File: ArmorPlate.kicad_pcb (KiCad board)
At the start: 2 copper layers, 134 x 124.5 mm, 47 parts, among them SW1 SW_Nidec_CAS-120A1, SW2 SW_Nidec_CAS-120A1

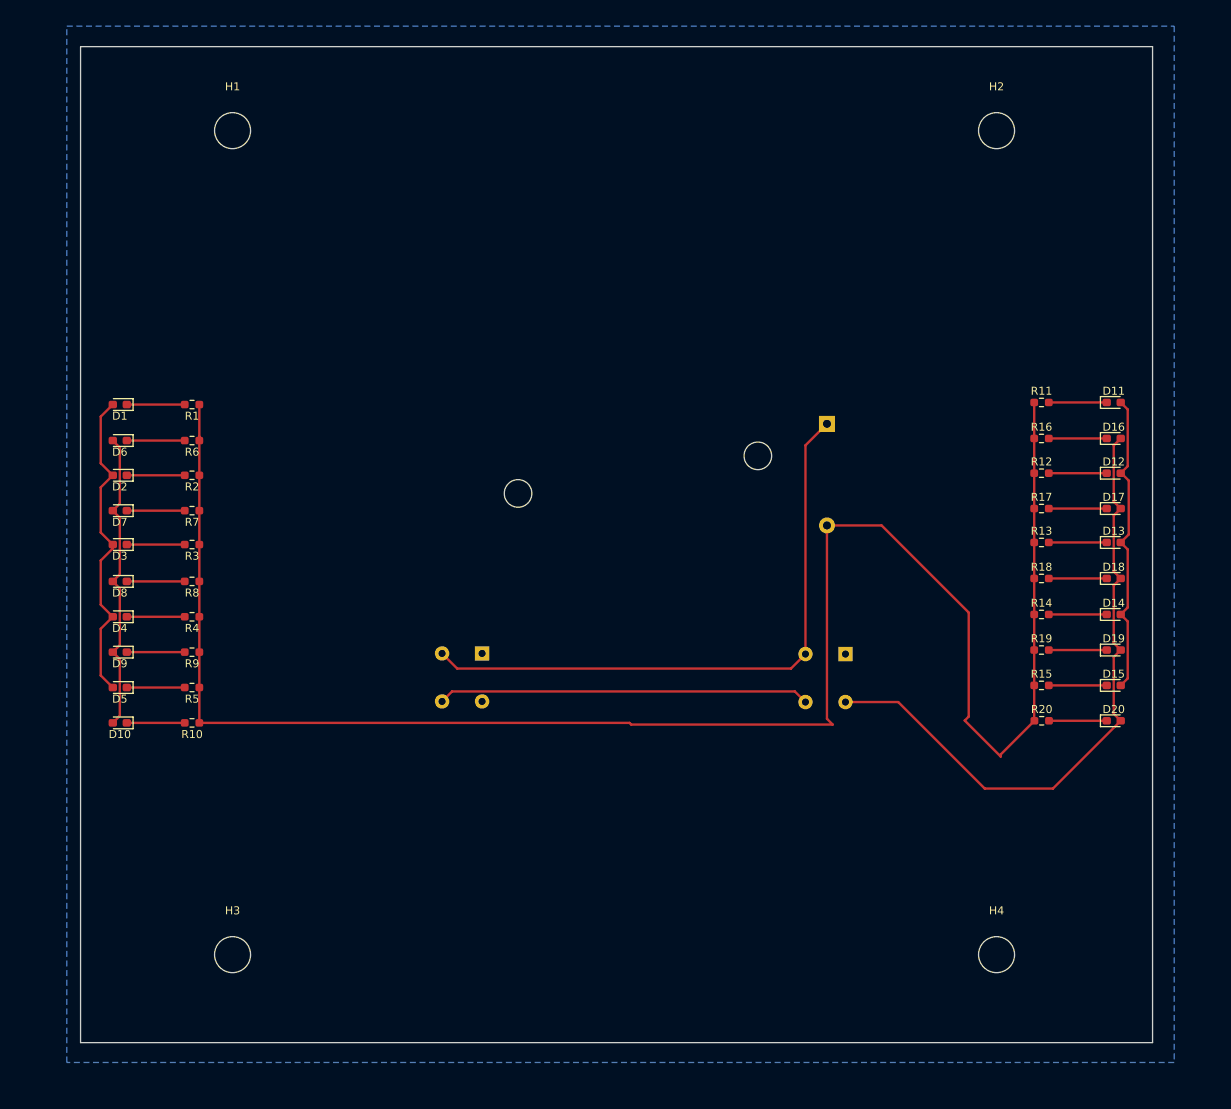
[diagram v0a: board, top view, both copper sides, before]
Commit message: updated pcb footprint for armorplate
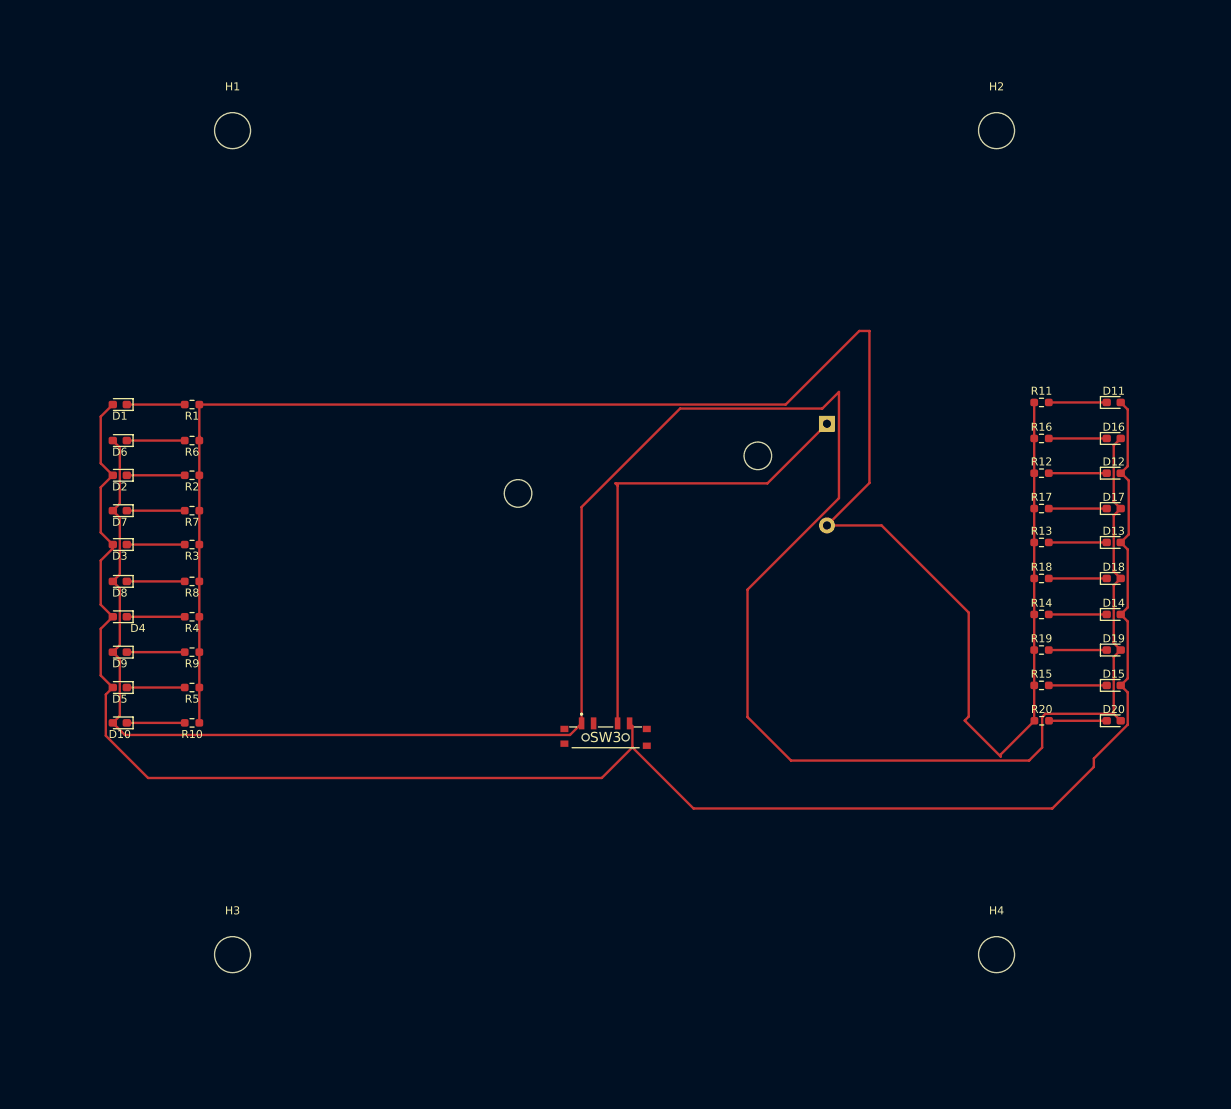
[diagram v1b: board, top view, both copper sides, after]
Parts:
- removed SW1, SW2: SW_Nidec_CAS-120A1, Button_Switch_THT:SW_Push_2P1T_Toggle_CK_PVA1xxH1xxxxxxV2
- added SW3: SW_SP3T, robomaster_footprints:EG1315AA, F.Cu at (148.6, 116.8)
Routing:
- net /3V blue: track 118.8 -> 299.4 mm
- net /3V Red: track 78.8 -> 233.2 mm
- net (no net): track 46.5 -> 0.00 mm
- net Net-(BT1-+): track 76.8 -> 59.6 mm
- net GND: track 233.1 -> 242.7 mm
- removed copper zone on B.Cu, net GND
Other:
- board outline removed

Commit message: final armorplate pcb with sp3t toggle switch
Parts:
- moved H2 0.89 mm to (196.9, 40.3)
- moved H1 0.89 mm to (102.5, 40.3)
- moved H4 0.89 mm to (196.9, 144.7)
- moved H3 0.89 mm to (102.5, 144.7)
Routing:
- added copper zone on B.Cu, net GND
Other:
- board outline added: 135 x 125.1 mm
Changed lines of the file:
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@@
 	(footprint "MountingHole:MountingHole_4.5mm"
 		(layer "F.Cu")
-		(at 102 144)
+		(at 102.55 144.7)
 		(descr "Mounting Hole 4.5mm, no annular")
 		(tags "mounting hole 4.5mm no annular")
@@
 	(footprint "MountingHole:MountingHole_4.5mm"
 		(layer "F.Cu")
-		(at 102 41)
+		(at 102.55 40.3)
 		(descr "Mounting Hole 4.5mm, no annular")
 		(tags "mounting hole 4.5mm no annular")
@@
 	(footprint "MountingHole:MountingHole_4.5mm"
 		(layer "F.Cu")
-		(at 197.5 41)
+		(at 196.95 40.3)
 		(descr "Mounting Hole 4.5mm, no annular")
 		(tags "mounting hole 4.5mm no annular")
@@
 	(footprint "MountingHole:MountingHole_4.5mm"
 		(layer "F.Cu")
-		(at 197.5 144)
+		(at 196.95 144.7)
 		(descr "Mounting Hole 4.5mm, no annular")
 		(tags "mounting hole 4.5mm no annular")
@@
 		)
 	)
+	(gr_arc
+		(start 217.55 150.745)
+		(mid 216.231981 153.926981)
+		(end 213.05 155.245)
+		(stroke
+			(width 0.05)
+			(type default)
+		)
+		(layer "Edge.Cuts")
+	)
+	(gr_arc
+		(start 213.05 30.175)
+		(mid 216.231981 31.493019)
+		(end 217.55 34.675)
+		(stroke
+			(width 0.05)
+			(type default)
+		)
+		(layer "Edge.Cuts")
+	)
+	(gr_line
+		(start 217.55 34.675)
+		(end 217.55 150.745)
+		(stroke
+			(width 0.05)
+			(type default)
+		)
+		(layer "Edge.Cuts")
+	)
+	(gr_line
+		(start 82.55 150.745)
+		(end 82.55 34.675)
+		(stroke
+			(width 0.05)
+			(type default)
+		)
+		(layer "Edge.Cuts")
+	)
+	(gr_arc
+		(start 82.55 34.675)
+		(mid 83.868019 31.493019)
+		(end 87.05 30.175)
+		(stroke
+			(width 0.05)
+			(type default)
+		)
+		(layer "Edge.Cuts")
+	)
+	(gr_line
+		(start 213.05 155.245)
+		(end 87.05 155.245)
+		(stroke
+			(width 0.05)
+			(type default)
+		)
+		(layer "Edge.Cuts")
+	)
+	(gr_line
+		(start 87.05 30.175)
+		(end 213.05 30.175)
+		(stroke
+			(width 0.05)
+			(type default)
+		)
+		(layer "Edge.Cuts")
+	)
+	(gr_arc
+		(start 87.05 155.245)
+		(mid 83.868019 153.926981)
+		(end 82.55 150.745)
+		(stroke
+			(width 0.05)
+			(type default)
+		)
+		(layer "Edge.Cuts")
+	)
 	(segment
 		(start 97.845 88.503337)
@@
 		(net 24)
 	)
+	(zone
+		(net 1)
+		(net_name "GND")
+		(layer "B.Cu")
+		(hatch edge 0.5)
+		(connect_pads
+			(clearance 0.5)
+		)
+		(min_thickness 0.25)
+		(filled_areas_thickness no)
+		(fill yes
+			(thermal_gap 0.5)
+			(thermal_bridge_width 0.5)
+		)
+		(polygon
+			(pts
+				(xy 74.93 26.67) (xy 74.93 161.29) (xy 224.79 161.29) (xy 224.79 26.67)
+			)
+		)
+	)
 )

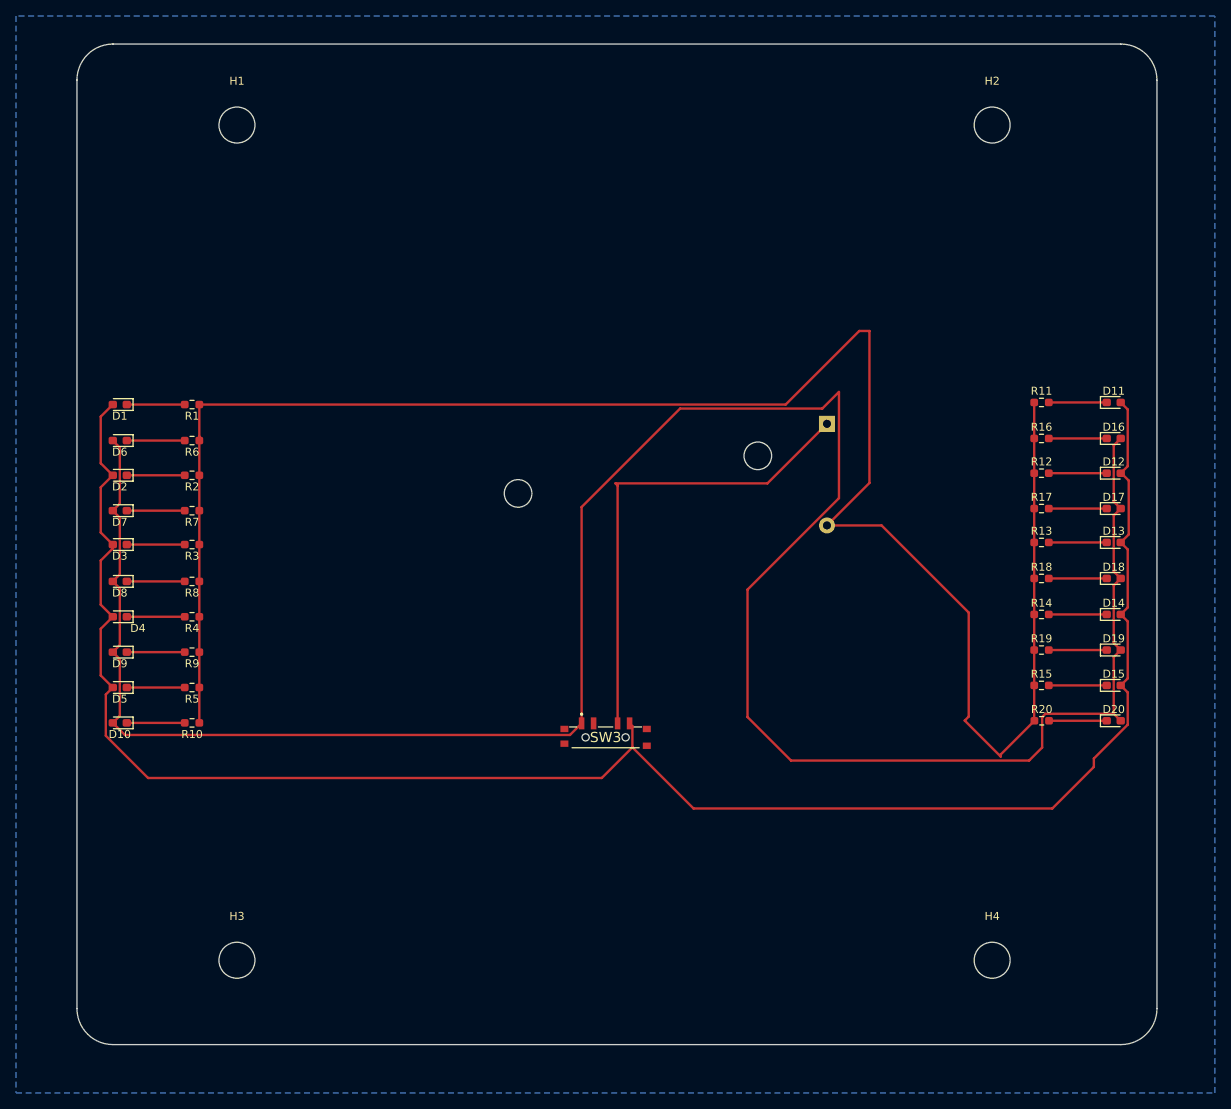
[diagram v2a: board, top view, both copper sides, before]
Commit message: fabrication files for armorplate
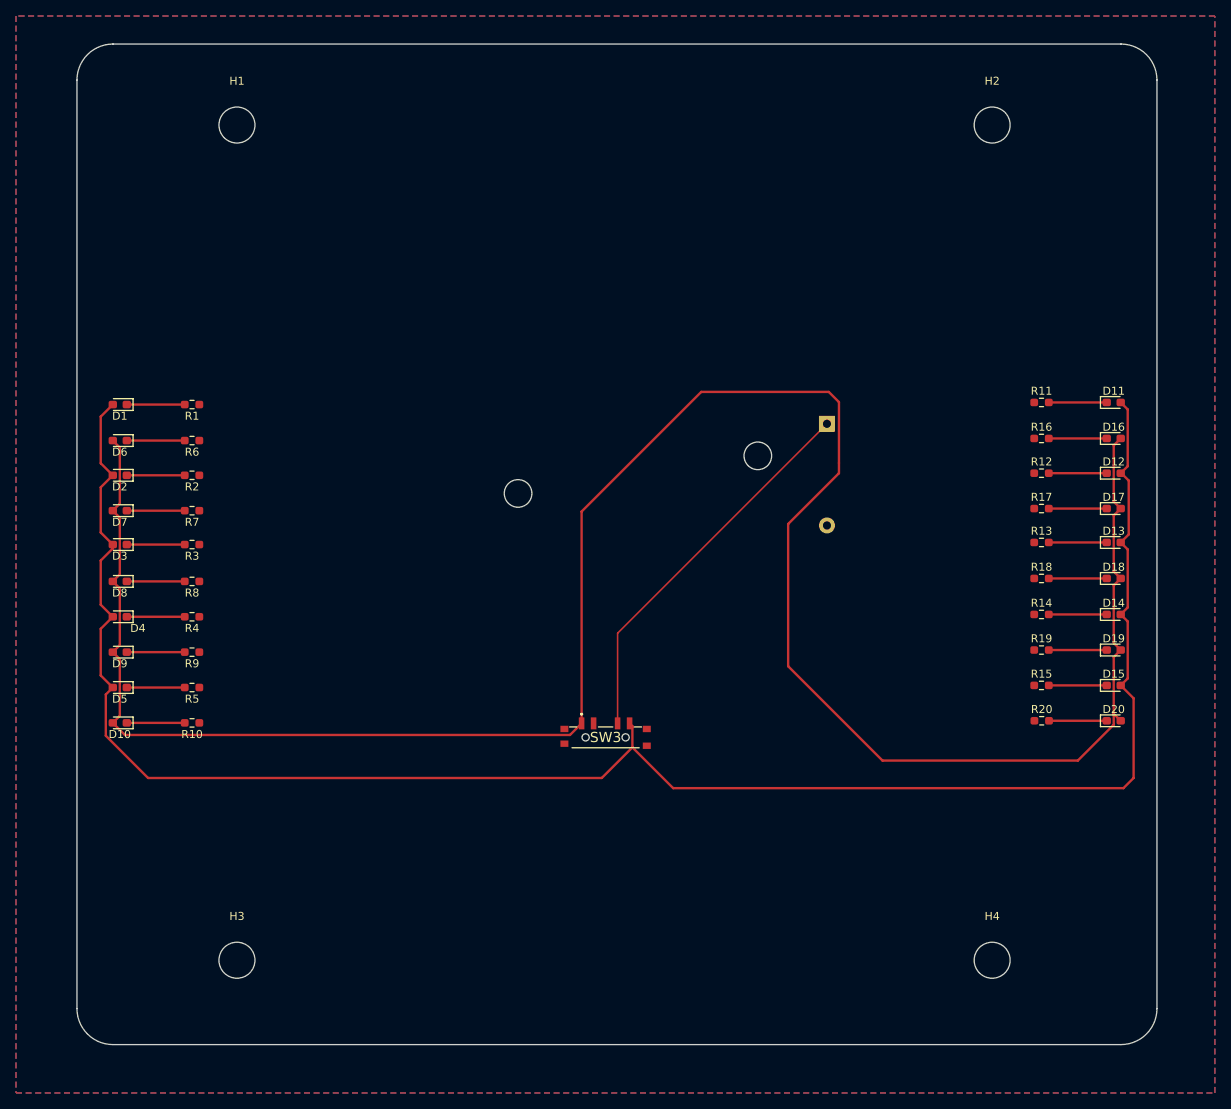
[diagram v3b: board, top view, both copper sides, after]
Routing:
- net GND: track 242.7 -> 0.00 mm
- net /3V blue: track 299.4 -> 286.0 mm
- net Net-(BT1-+): track 59.6 -> 48.3 mm
- net /3V Red: track 233.2 -> 235.5 mm
- added copper zone on F.Cu, net GND
